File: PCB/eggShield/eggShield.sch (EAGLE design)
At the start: 54 parts, among them J2 AVR_SPI_PRG_6NS, U1 V_REG_LDOSMD, U2 V_REG_LDOSMD, U3 MCP42XXX

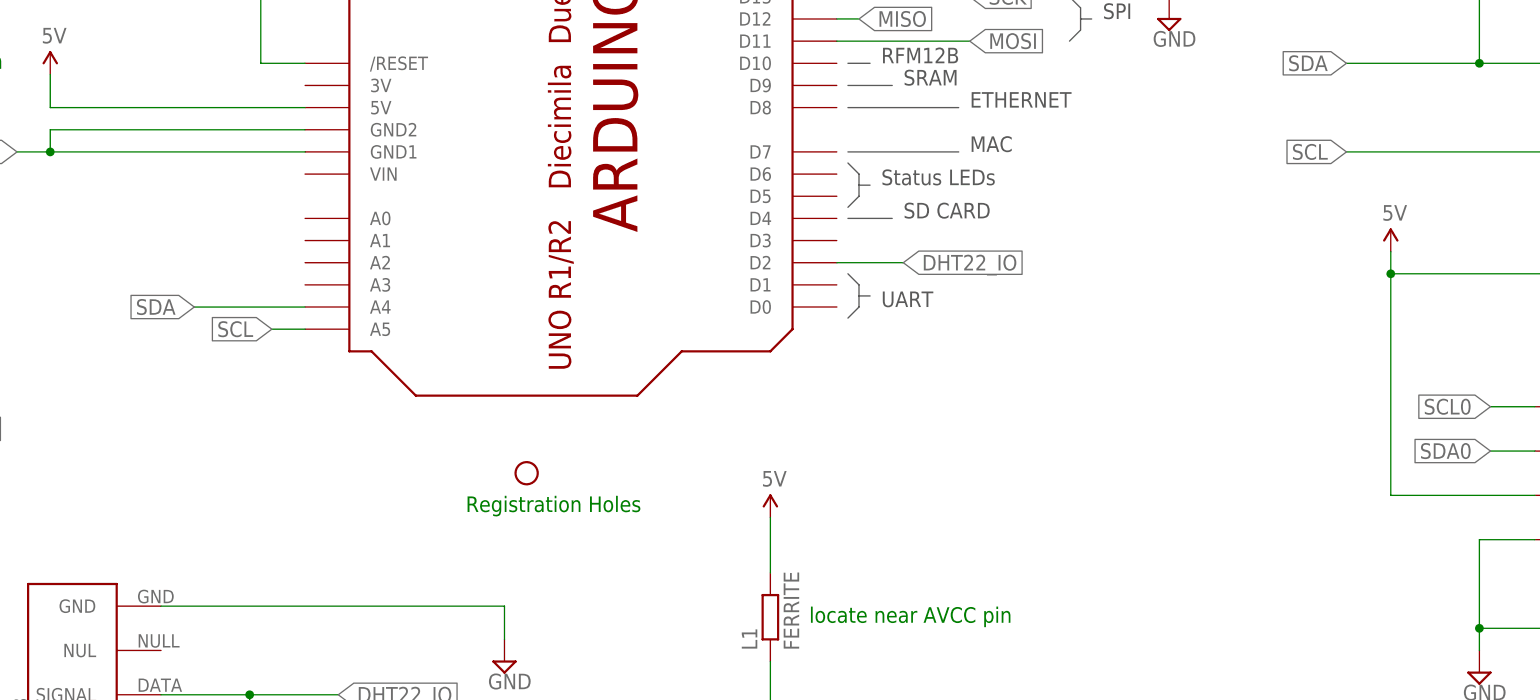
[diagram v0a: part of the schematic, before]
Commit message: added barrel jack to shield for 7-15V external power to NAnode
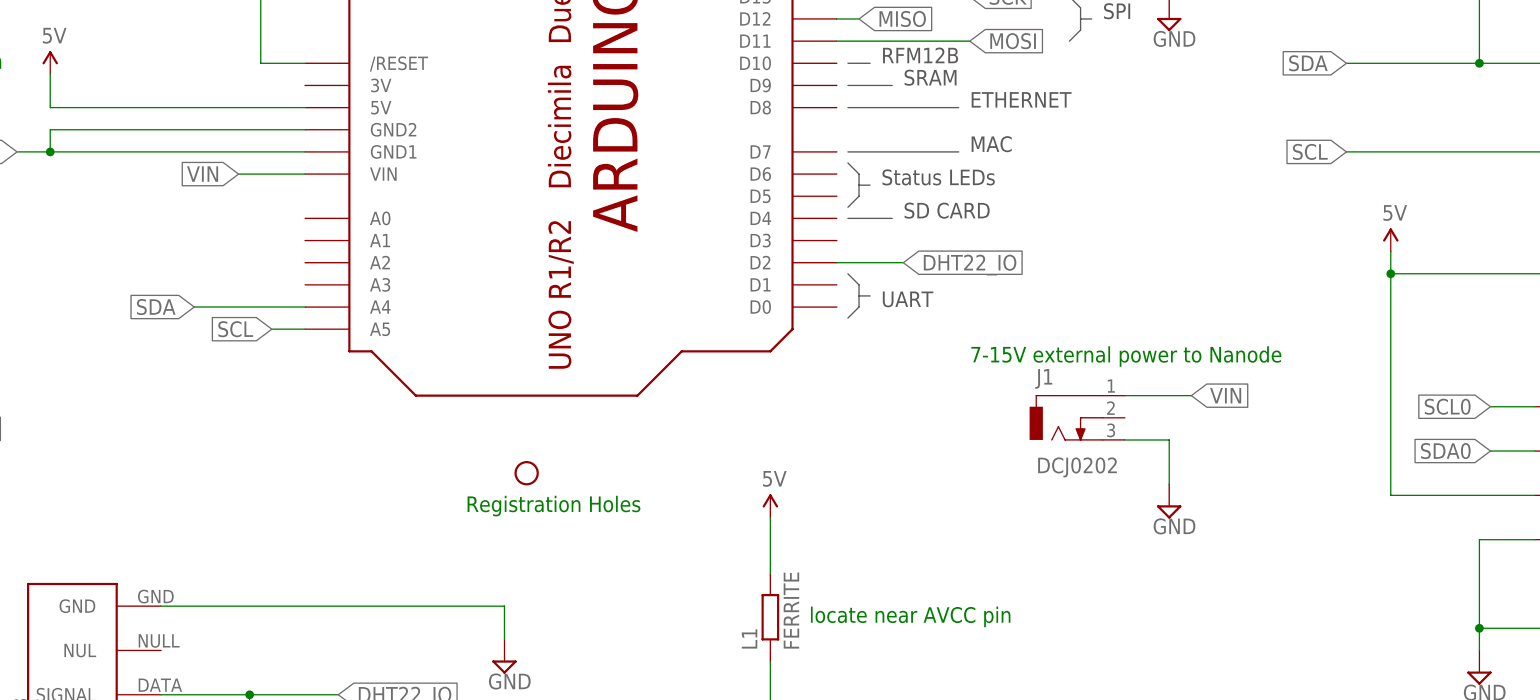
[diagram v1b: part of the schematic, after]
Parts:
- added J1: DCJ0202, con-jack:DCJ0202
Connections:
- new net VIN: J1.1, U$7.VIN
- net GND: now also J1.3
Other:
- note added: "7-15V external power to Nanode"
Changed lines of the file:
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@@
 <part name="SUPPLY6" library="supply2" deviceset="GND" device=""/>
 <part name="U$17" library="SparkFun" deviceset="5V" device=""/>
+<part name="J1" library="con-jack" deviceset="DCJ0202" device=""/>
+<part name="SUPPLY2" library="supply2" deviceset="GND" device=""/>
 </parts>
 <sheets>
@@
 <text x="74.295" y="94.615" size="1.778" layer="91">2.5V</text>
 <text x="330.2" y="102.87" size="1.778" layer="91">programming header</text>
+<text x="223.52" y="176.53" size="1.778" layer="91">7-15V external power to Nanode</text>
 </plain>
 <instances>
@@
 <instance part="SUPPLY6" gate="GND" x="364.49" y="106.68"/>
 <instance part="U$17" gate="G$1" x="364.49" y="130.81"/>
+<instance part="J1" gate="G$1" x="233.68" y="170.18"/>
+<instance part="SUPPLY2" gate="GND" x="246.38" y="160.02"/>
 </instances>
 <busses>
@@
 <wire x1="364.49" y1="118.11" x2="364.49" y2="109.22" width="0.1524" layer="91"/>
 </segment>
+<segment>
+<pinref part="J1" gate="G$1" pin="3"/>
+<wire x1="241.3" y1="167.64" x2="246.38" y2="167.64" width="0.1524" layer="91"/>
+<wire x1="246.38" y1="167.64" x2="246.38" y2="162.56" width="0.1524" layer="91"/>
+<pinref part="SUPPLY2" gate="GND" pin="GND"/>
+</segment>
 </net>
 <net name="CO_RH-" class="0">
@@
 </segment>
 </net>
+<net name="VIN" class="0">
+<segment>
+<pinref part="U$7" gate="G$1" pin="VIN"/>
+<wire x1="147.32" y1="198.12" x2="139.7" y2="198.12" width="0.1524" layer="91"/>
+<label x="139.7" y="198.12" size="1.778" layer="95" rot="R180" xref="yes"/>
+</segment>
+<segment>
+<pinref part="J1" gate="G$1" pin="1"/>
+<wire x1="241.3" y1="172.72" x2="248.92" y2="172.72" width="0.1524" layer="91"/>
+<label x="248.92" y="172.72" size="1.778" layer="95" xref="yes"/>
+</segment>
+</net>

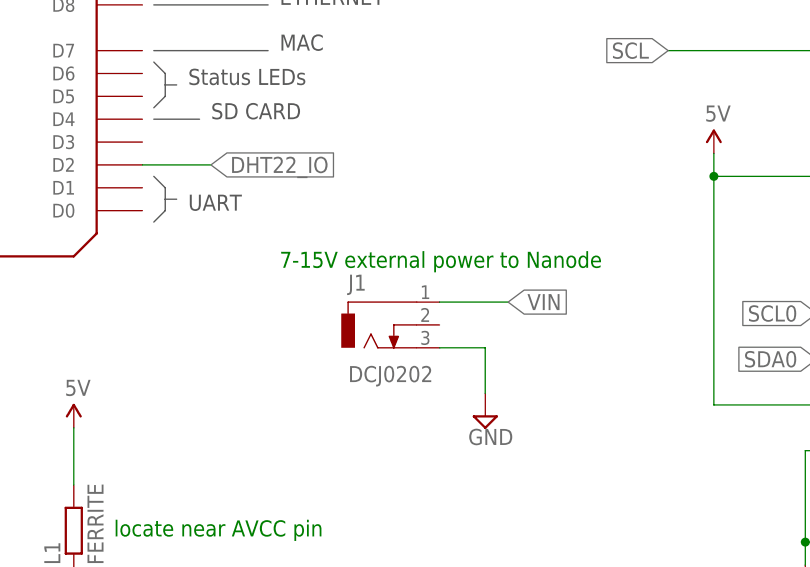
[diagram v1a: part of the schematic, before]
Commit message: added silk screen to barrel jack to make voltage input range and polarity clear
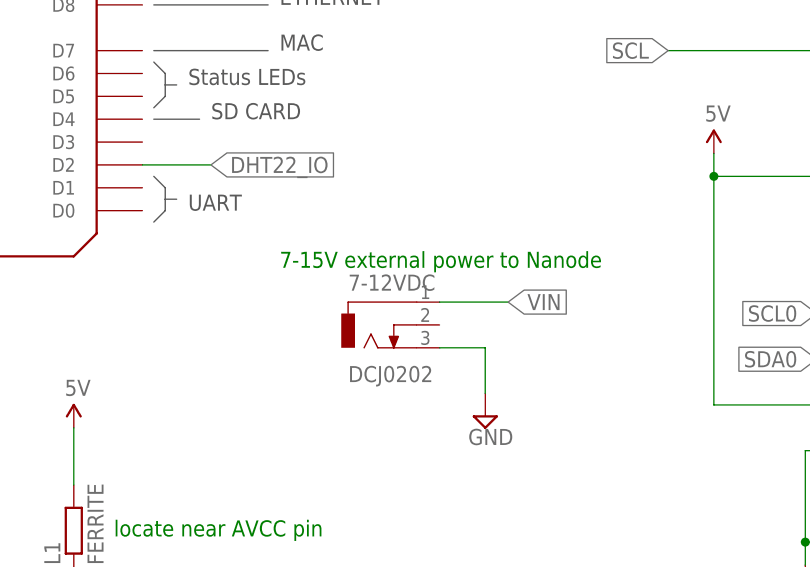
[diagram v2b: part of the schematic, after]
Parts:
- renumbered J1 to 7-12VDC
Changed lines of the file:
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@@
 <setting verticaltext="up"/>
 </settings>
-<grid distance="0.05" unitdist="inch" unit="inch" style="lines" multiple="1" display="no" altdistance="0.01" altunitdist="inch" altunit="inch"/>
+<grid distance="0.1" unitdist="inch" unit="inch" style="lines" multiple="1" display="no" altdistance="0.01" altunitdist="inch" altunit="inch"/>
 <layers>
 <layer number="1" name="Top" color="4" fill="1" visible="no" active="no"/>
@@
 <part name="SUPPLY6" library="supply2" deviceset="GND" device=""/>
 <part name="U$17" library="SparkFun" deviceset="5V" device=""/>
-<part name="J1" library="con-jack" deviceset="DCJ0202" device=""/>
+<part name="7-12VDC" library="con-jack" deviceset="DCJ0202" device=""/>
 <part name="SUPPLY2" library="supply2" deviceset="GND" device=""/>
 </parts>
@@
 <instance part="SUPPLY6" gate="GND" x="364.49" y="106.68"/>
 <instance part="U$17" gate="G$1" x="364.49" y="130.81"/>
-<instance part="J1" gate="G$1" x="233.68" y="170.18"/>
+<instance part="7-12VDC" gate="G$1" x="233.68" y="170.18"/>
 <instance part="SUPPLY2" gate="GND" x="246.38" y="160.02"/>
 </instances>
@@
 </segment>
 <segment>
-<pinref part="J1" gate="G$1" pin="3"/>
+<pinref part="7-12VDC" gate="G$1" pin="3"/>
 <wire x1="241.3" y1="167.64" x2="246.38" y2="167.64" width="0.1524" layer="91"/>
 <wire x1="246.38" y1="167.64" x2="246.38" y2="162.56" width="0.1524" layer="91"/>
@@
 </segment>
 <segment>
-<pinref part="J1" gate="G$1" pin="1"/>
+<pinref part="7-12VDC" gate="G$1" pin="1"/>
 <wire x1="241.3" y1="172.72" x2="248.92" y2="172.72" width="0.1524" layer="91"/>
 <label x="248.92" y="172.72" size="1.778" layer="95" xref="yes"/>

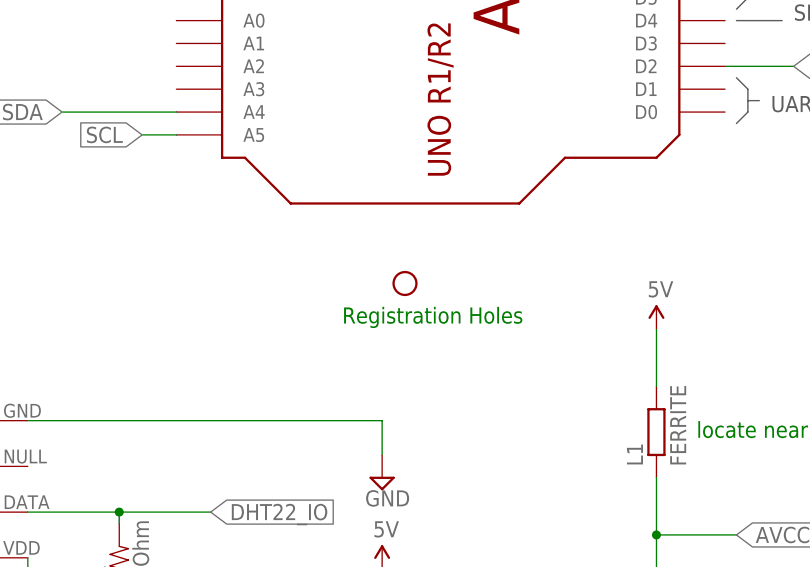
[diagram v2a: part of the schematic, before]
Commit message: deleted registration hole that was sitting out in the middle of nowhere
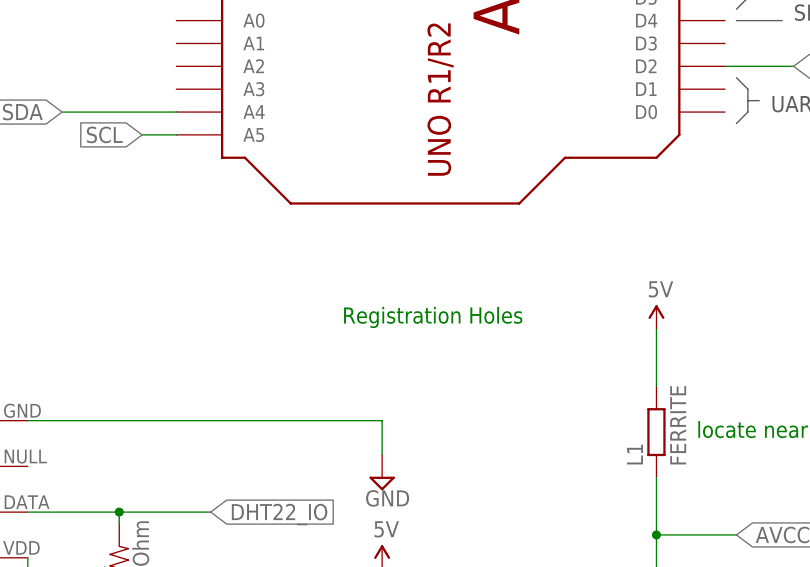
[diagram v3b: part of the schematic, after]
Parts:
- removed JP3: STAND-OFF, SparkFun:STAND-OFF
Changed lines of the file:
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@@
 <part name="BUS2.1" library="wicked-device" deviceset="4-PIN-SMT" device=""/>
 <part name="SUPPLY11" library="supply2" deviceset="GND" device=""/>
-<part name="JP3" library="SparkFun" deviceset="STAND-OFF" device=""/>
 <part name="R14" library="SparkFun" deviceset="RESISTOR" device="0805-RES" value="1.8kOhm"/>
 <part name="R15" library="SparkFun" deviceset="RESISTOR" device="0805-RES" value="1.8kOhm"/>
@@
 <instance part="BUS2.1" gate="G$1" x="412.75" y="163.83"/>
 <instance part="SUPPLY11" gate="GND" x="281.94" y="140.97"/>
-<instance part="JP3" gate="G$1" x="172.72" y="163.83"/>
 <instance part="R14" gate="G$1" x="373.38" y="256.54" rot="R90"/>
 <instance part="R15" gate="G$1" x="383.54" y="256.54" rot="R90"/>

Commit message: routed DHT22 to A3
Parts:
- R1: value (none) -> 2.2kOhm
- R10: value (none) -> 680kOhm
- R18, R19: value (none) -> 68Ohm
- R2: value (none) -> 22kOhm
- R3: value (none) -> 220kOhm
- R4: value 1.8MOhm -> 120kOhm
- R6, R9: value (none) -> 68kOhm
- R7: value 750kOhm -> 56kOhm
- R8: value 470ohm -> 270ohm
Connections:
- net DHT22_IO: now also U$7.A3; no longer U$7.D2
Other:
- note added: "RFM12 /INT"
- note added: "RTC /INT"
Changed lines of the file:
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@@
 <part name="C4" library="wicked-device" deviceset="EEE-1EA100WR" device="" value="10uF"/>
 <part name="N02" library="ricardo" deviceset="E2V" device=""/>
-<part name="R1" library="SparkFun" deviceset="RESISTOR" device="0805-RES"/>
-<part name="R4" library="SparkFun" deviceset="RESISTOR" device="0805-RES" value="1.8MOhm"/>
+<part name="R1" library="SparkFun" deviceset="RESISTOR" device="0805-RES" value="2.2kOhm"/>
+<part name="R4" library="SparkFun" deviceset="RESISTOR" device="0805-RES" value="120kOhm"/>
 <part name="U1" library="SparkFun" deviceset="V_REG_LDO" device="SMD"/>
-<part name="R2" library="SparkFun" deviceset="RESISTOR" device="0805-RES"/>
-<part name="R3" library="SparkFun" deviceset="RESISTOR" device="0805-RES"/>
+<part name="R2" library="SparkFun" deviceset="RESISTOR" device="0805-RES" value="22kOhm"/>
+<part name="R3" library="SparkFun" deviceset="RESISTOR" device="0805-RES" value="220kOhm"/>
 <part name="SUPPLY9" library="supply2" deviceset="GND" device=""/>
 <part name="C8" library="SparkFun" deviceset="CAP" device="0603-CAP" value="0.1uF"/>
 <part name="C9" library="wicked-device" deviceset="EEE-1EA100WR" device="" value="10uF"/>
-<part name="R7" library="SparkFun" deviceset="RESISTOR" device="0805-RES" value="750kOhm"/>
+<part name="R7" library="SparkFun" deviceset="RESISTOR" device="0805-RES" value="56kOhm"/>
 <part name="U2" library="SparkFun" deviceset="V_REG_LDO" device="SMD"/>
 <part name="CO" library="ricardo" deviceset="E2V" device=""/>
-<part name="R6" library="SparkFun" deviceset="RESISTOR" device="0805-RES"/>
-<part name="R9" library="SparkFun" deviceset="RESISTOR" device="0805-RES"/>
-<part name="R10" library="SparkFun" deviceset="RESISTOR" device="0805-RES"/>
+<part name="R6" library="SparkFun" deviceset="RESISTOR" device="0805-RES" value="68kOhm"/>
+<part name="R9" library="SparkFun" deviceset="RESISTOR" device="0805-RES" value="68kOhm"/>
+<part name="R10" library="SparkFun" deviceset="RESISTOR" device="0805-RES" value="680kOhm"/>
 <part name="DHT22" library="ricardo" deviceset="RHT03" device=""/>
 <part name="U$7" library="adafruit" deviceset="ARDUINO" device="-NOHOLE"/>
@@
 <part name="R17" library="SparkFun" deviceset="RESISTOR" device="0805-RES" value="1.8kOhm"/>
 <part name="U3" library="SparkFun-AnalogIC" deviceset="MCP42XXX" device=""/>
-<part name="R18" library="SparkFun" deviceset="RESISTOR" device="0805-RES"/>
-<part name="R19" library="SparkFun" deviceset="RESISTOR" device="0805-RES"/>
+<part name="R18" library="SparkFun" deviceset="RESISTOR" device="0805-RES" value="68Ohm"/>
+<part name="R19" library="SparkFun" deviceset="RESISTOR" device="0805-RES" value="68Ohm"/>
 <part name="SUPPLY12" library="supply2" deviceset="GND" device=""/>
 <part name="C7" library="SparkFun" deviceset="CAP" device="0603-CAP" value="0.1uF"/>
@@
 <part name="R5" library="SparkFun" deviceset="RESISTOR" device="0805-RES" value="270ohm"/>
 <part name="PWR" library="adafruit" deviceset="LED" device="CHIPLED_0805" value="RED"/>
-<part name="R8" library="SparkFun" deviceset="RESISTOR" device="0805-RES" value="470ohm"/>
+<part name="R8" library="SparkFun" deviceset="RESISTOR" device="0805-RES" value="270ohm"/>
 <part name="SUPPLY4" library="supply2" deviceset="GND" device=""/>
 <part name="VCC2_5" library="wicked-device" deviceset="AP7333" device="SA"/>
@@
 <text x="223.52" y="205.74" size="1.778" layer="97">ETHERNET</text>
 <text x="215.9" y="193.04" size="1.778" layer="97">SD CARD</text>
-<wire x1="209.55" y1="200.66" x2="222.25" y2="200.66" width="0.1524" layer="97"/>
+<wire x1="210.82" y1="200.66" x2="222.25" y2="200.66" width="0.1524" layer="97"/>
 <text x="223.52" y="200.66" size="1.778" layer="97">MAC</text>
 <wire x1="209.55" y1="199.39" x2="210.82" y2="198.12" width="0.1524" layer="97"/>
@@
 <text x="330.2" y="102.87" size="1.778" layer="91">programming header</text>
 <text x="223.52" y="176.53" size="1.778" layer="91">7-15V external power to Nanode</text>
+<text x="213.487" y="187.1472" size="1.778" layer="97">RFM12 /INT</text>
+<text x="213.5124" y="189.8904" size="1.778" layer="97">RTC /INT</text>
+<wire x1="209.4738" y1="190.4746" x2="212.3694" y2="190.4746" width="0.1524" layer="97"/>
+<wire x1="209.423" y1="187.9854" x2="213.0298" y2="187.9854" width="0.1524" layer="97"/>
 </plain>
 <instances>
@@
 <segment>
 <pinref part="U$7" gate="G$1" pin="A4"/>
-<wire x1="147.32" y1="182.88" x2="134.62" y2="182.88" width="0.1524" layer="91"/>
-<label x="134.62" y="182.88" size="1.778" layer="95" rot="R180" xref="yes"/>
+<wire x1="147.32" y1="182.88" x2="144.78" y2="182.88" width="0.1524" layer="91"/>
+<label x="144.78" y="182.88" size="1.778" layer="95" rot="R180" xref="yes"/>
 </segment>
 <segment>
@@
 <segment>
 <pinref part="U$7" gate="G$1" pin="A5"/>
-<wire x1="147.32" y1="180.34" x2="143.51" y2="180.34" width="0.1524" layer="91"/>
-<label x="143.51" y="180.34" size="1.778" layer="95" rot="R180" xref="yes"/>
+<wire x1="147.32" y1="180.34" x2="133.35" y2="180.34" width="0.1524" layer="91"/>
+<label x="133.35" y="180.34" size="1.778" layer="95" rot="R180" xref="yes"/>
 </segment>
 <segment>
@@
 <net name="DHT22_IO" class="0">
 <segment>
-<pinref part="U$7" gate="G$1" pin="D2"/>
-<wire x1="208.28" y1="187.96" x2="215.9" y2="187.96" width="0.1524" layer="91"/>
-<label x="215.9" y="187.96" size="1.778" layer="95" xref="yes"/>
-</segment>
-<segment>
 <pinref part="DHT22" gate="G$1" pin="SIGNAL"/>
 <wire x1="130.81" y1="138.43" x2="140.97" y2="138.43" width="0.1524" layer="91"/>
@@
 <pinref part="R11" gate="G$1" pin="2"/>
 </segment>
-</net>
+<segment>
+<label x="134.62" y="185.42" size="1.778" layer="95" rot="R180" xref="yes"/>
+<pinref part="U$7" gate="G$1" pin="A3"/>
+<wire x1="134.62" y1="185.42" x2="147.32" y2="185.42" width="0.1524" layer="91"/>
+</segment>
+</net>

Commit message: fixed 2.5v regulator bug
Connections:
- removed net N$2: C11.1, VCC2_5.VI
- net 5V: now also C11.1, VCC2_5.VI
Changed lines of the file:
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@@
 <setting verticaltext="up"/>
 </settings>
-<grid distance="0.1" unitdist="inch" unit="inch" style="lines" multiple="1" display="no" altdistance="0.01" altunitdist="inch" altunit="inch"/>
+<grid distance="0.05" unitdist="inch" unit="inch" style="lines" multiple="1" display="no" altdistance="0.01" altunitdist="inch" altunit="inch"/>
 <layers>
 <layer number="1" name="Top" color="4" fill="1" visible="no" active="no"/>
@@
 <part name="7-12VDC" library="con-jack" deviceset="DCJ0202" device=""/>
 <part name="SUPPLY2" library="supply2" deviceset="GND" device=""/>
+<part name="U$18" library="SparkFun" deviceset="5V" device=""/>
 </parts>
 <sheets>
@@
 <instance part="7-12VDC" gate="G$1" x="233.68" y="170.18"/>
 <instance part="SUPPLY2" gate="GND" x="246.38" y="160.02"/>
+<instance part="U$18" gate="G$1" x="43.18" y="22.86"/>
 </instances>
 <busses>
@@
 <pinref part="U$17" gate="G$1" pin="5V"/>
 </segment>
+<segment>
+<pinref part="VCC2_5" gate="G$1" pin="VI"/>
+<wire x1="54.61" y1="20.32" x2="48.26" y2="20.32" width="0.1524" layer="91"/>
+<pinref part="C11" gate="G$1" pin="1"/>
+<wire x1="48.26" y1="20.32" x2="48.26" y2="17.78" width="0.1524" layer="91"/>
+<wire x1="48.26" y1="20.32" x2="43.18" y2="20.32" width="0.1524" layer="91"/>
+<junction x="48.26" y="20.32"/>
+<wire x1="43.18" y1="20.32" x2="43.18" y2="22.86" width="0.1524" layer="91"/>
+<pinref part="U$18" gate="G$1" pin="5V"/>
+</segment>
 </net>
 <net name="AVCC" class="0">
@@
 </segment>
 </net>
-<net name="N$2" class="0">
-<segment>
-<pinref part="VCC2_5" gate="G$1" pin="VI"/>
-<wire x1="54.61" y1="20.32" x2="48.26" y2="20.32" width="0.1524" layer="91"/>
-<pinref part="C11" gate="G$1" pin="1"/>
-<wire x1="48.26" y1="20.32" x2="48.26" y2="17.78" width="0.1524" layer="91"/>
-</segment>
-</net>

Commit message: updates to the initial prototype based on testing and feedback. Fixed crossed up digipot lines, rotated the DHT22, move the barrel jack off the headers, replaced 0603s with 0805s.
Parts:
- added MAC: 11AA02E48, nanode:11AA02E48
- C1, C10, C11, C12, C2, C3, C5, C6, C7, C8: device SparkFun:CAP0603-CAP -> SparkFun-Passives:CAP0805
- L1: device nanodeRF_11:RCL_R-EU_R0805 -> SparkFun-Passives:INDUCTOR0805
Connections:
- removed net N$4: C1.2, U$7.AREF
- new net MAC_IO: MAC.SCIO, MCU.PD7(PCINT23/AIN1)
- net 5V: now also C1.1, MAC.VCC
- net CO_RH-: now also U3.W0; no longer U3.W1
- net GND: now also 7-12VDC.2, C1.2, MAC.VSS; no longer C1.1
- net NO2_RH-: now also U3.W1; no longer U3.W0
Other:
- note added: "MAC/EEPROM Chip (for ID and possibly Calibration Data)"
- note removed: "locate near AREF pin"
- moved on the sheet: C1
